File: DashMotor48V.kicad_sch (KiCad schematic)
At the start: 105 parts, among them CN3(OUT)1 XT30(2+2)PB-M.G.B, CN3(OUT)2 XT30(2+2)PB-M.G.B, J1 JST BM07B-SRSS-TB(LF)(SN), J2 JST BM07B-SRSS-TB(LF)(SN), Q1 FDMS039N08B, Q2 FDMS039N08B, Q3 FDMS039N08B, Q4 FDMS039N08B, Q5 FDMS039N08B, Q6 FDMS039N08B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

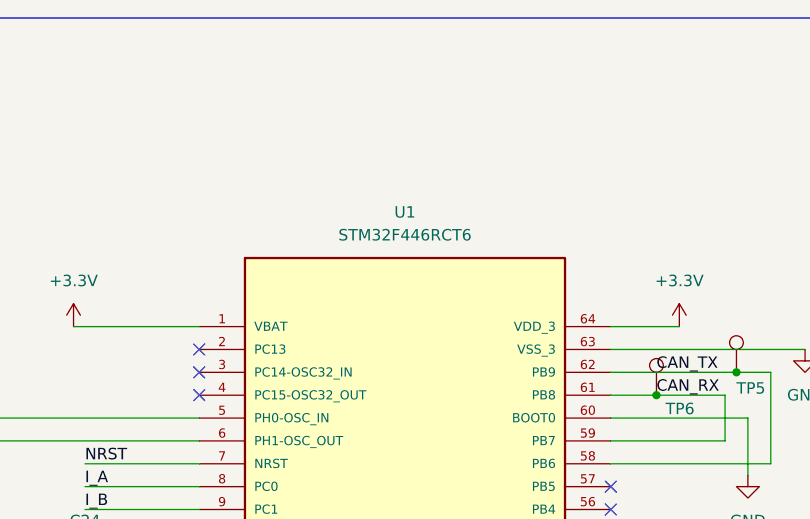
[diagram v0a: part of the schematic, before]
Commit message: noticed they have stm32f446ret, will use that
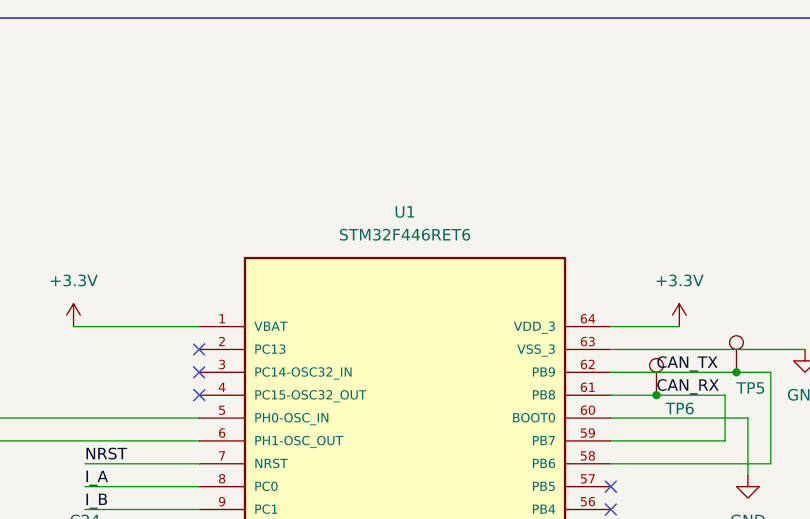
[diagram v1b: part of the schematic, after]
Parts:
- U1: value STM32F446RCT6 -> STM32F446RET6
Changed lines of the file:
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@@
 			)
 		)
-		(property "Value" "STM32F446RCT6"
+		(property "Value" "STM32F446RET6"
 			(at 125.73 43.18 0)
 			(effects
@@
 			)
 		)
-		(property "Description" ""
+		(property "Description" "I found out they have RET6 now"
 			(at 125.73 111.76 0)
 			(effects

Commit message: version sent to production
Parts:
- C37: value 2.2uF -> CL31B225KCHSNNE
- J1, J2: value JST BM07B-SRSS-TB(LF)(SN) -> BM07B-SRSS-TB(LF)(SN)
- L2, L3: value 2.2uH -> DFE252012PD-2R2M=P2
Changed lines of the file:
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@@
 			)
 		)
-		(property "Value" "2.2uF"
+		(property "Value" "CL31B225KCHSNNE"
 			(at 41.91 309.8799 90)
 			(effects
@@
 			)
 		)
-		(property "Description" ""
+		(property "Description" "2.2uF"
 			(at 38.1 309.88 0)
 			(effects
@@
 		(dnp no)
 		(property "Reference" "C42"
-			(at 123.19 314.9599 0)
+			(at 123.19 316.992 0)
 			(effects
 				(font
@@
 			)
 		)
-		(property "Value" "2.2uH"
+		(property "Value" "DFE252012PD-2R2M=P2"
 			(at 369.57 313.69 0)
 			(effects
@@
 					(size 1.27 1.27)
 				)
+				(hide yes)
 			)
 		)
@@
 			)
 		)
-		(property "Description" ""
+		(property "Description" "2.2uH"
 			(at 369.57 317.5 0)
 			(effects
@@
 					(size 1.27 1.27)
 				)
-				(hide yes)
 			)
 		)
@@
 			)
 		)
-		(property "Value" "JST BM07B-SRSS-TB(LF)(SN)"
+		(property "Value" "BM07B-SRSS-TB(LF)(SN)"
 			(at 430.784 264.668 0)
 			(effects
@@
 		(dnp no)
 		(property "Reference" "C43"
-			(at 128.27 300.99 90)
+			(at 128.016 303.53 90)
 			(effects
 				(font
@@
 			)
 		)
-		(property "Value" "2.2uH"
+		(property "Value" "DFE252012PD-2R2M=P2"
 			(at 260.35 313.69 0)
 			(effects
@@
 					(size 1.27 1.27)
 				)
+				(hide yes)
 			)
 		)
@@
 			)
 		)
-		(property "Description" ""
+		(property "Description" "2.2uH"
 			(at 260.35 317.5 0)
 			(effects
@@
 					(size 1.27 1.27)
 				)
-				(hide yes)
 			)
 		)
@@
 			)
 		)
-		(property "Value" "JST BM07B-SRSS-TB(LF)(SN)"
+		(property "Value" "BM07B-SRSS-TB(LF)(SN)"
 			(at 386.334 264.668 0)
 			(effects
